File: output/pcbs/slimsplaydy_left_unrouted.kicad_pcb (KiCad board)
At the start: 2 copper layers, 117.1 x 87.4 mm, 24 parts

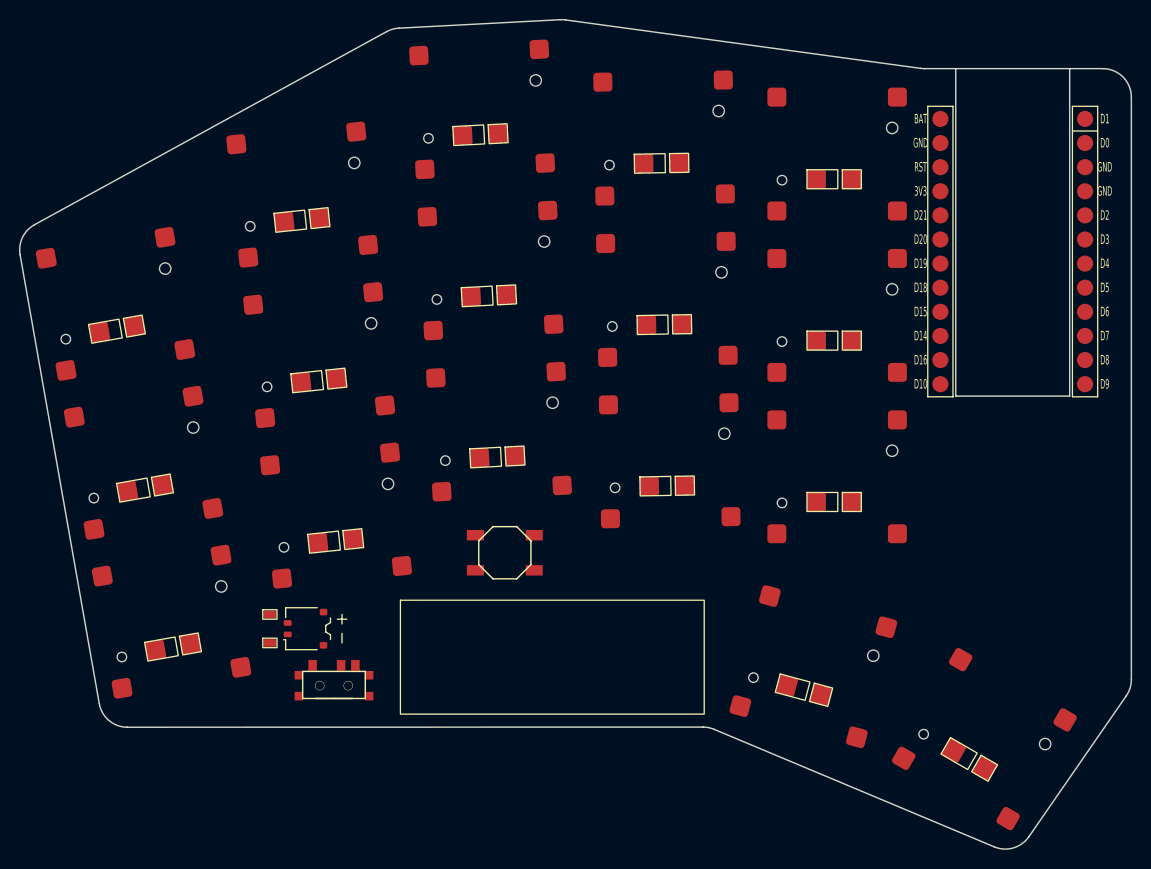
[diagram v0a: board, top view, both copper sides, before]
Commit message: Change weird 5/28 roundrect ratios to 1/8
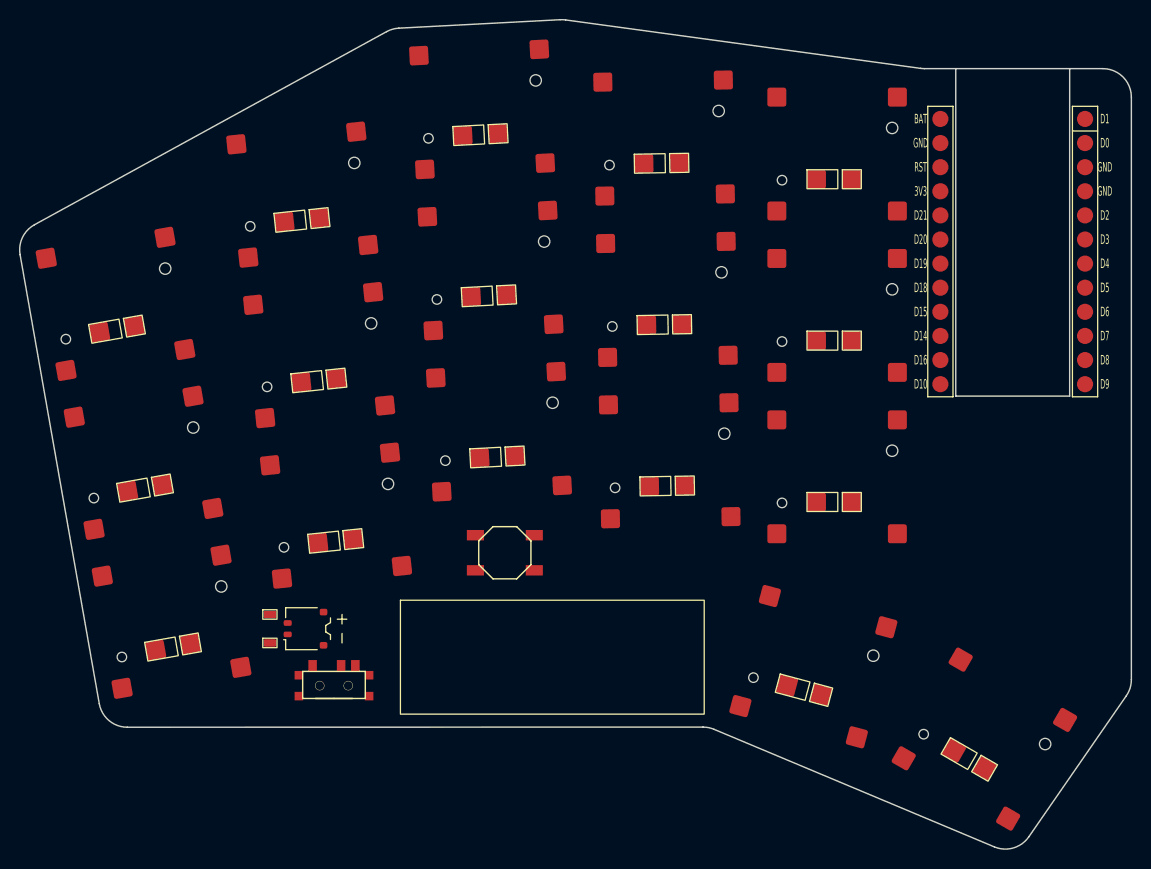
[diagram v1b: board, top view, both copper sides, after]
